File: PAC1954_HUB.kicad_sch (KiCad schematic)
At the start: 11 parts, among them U25 PAC1954T-E_4MX

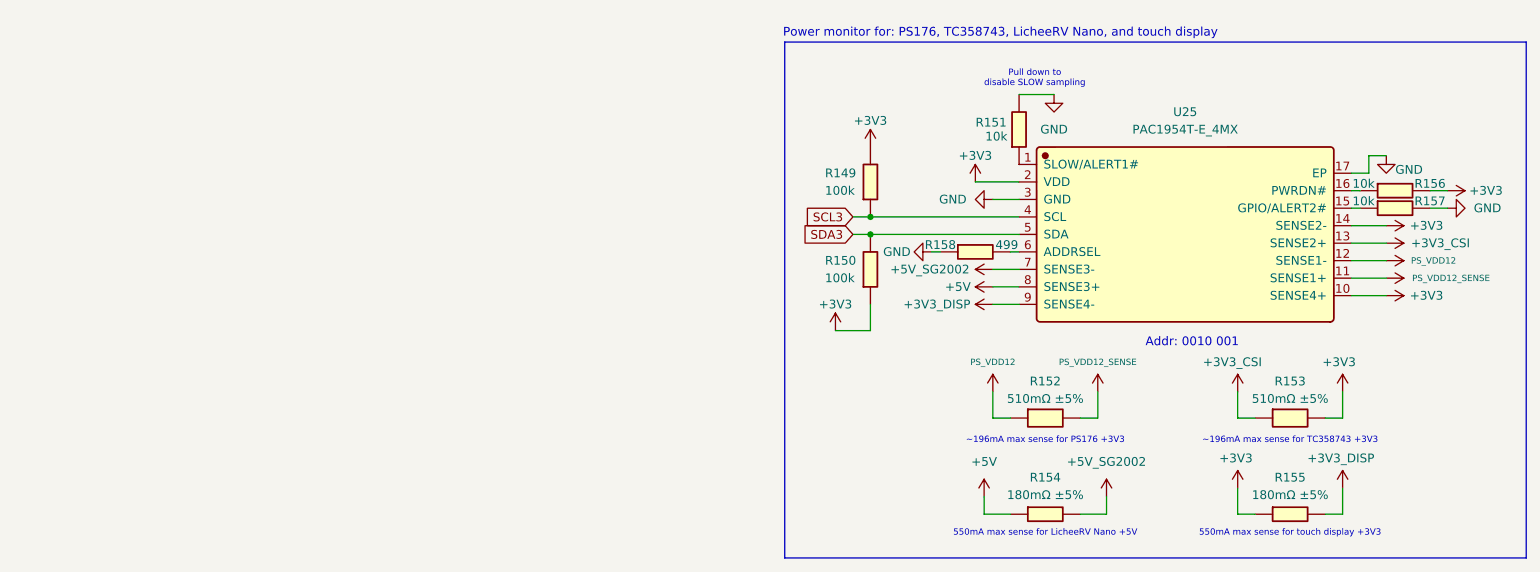
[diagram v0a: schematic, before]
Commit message: Mostly complete initial transfer to hierarchical schematic
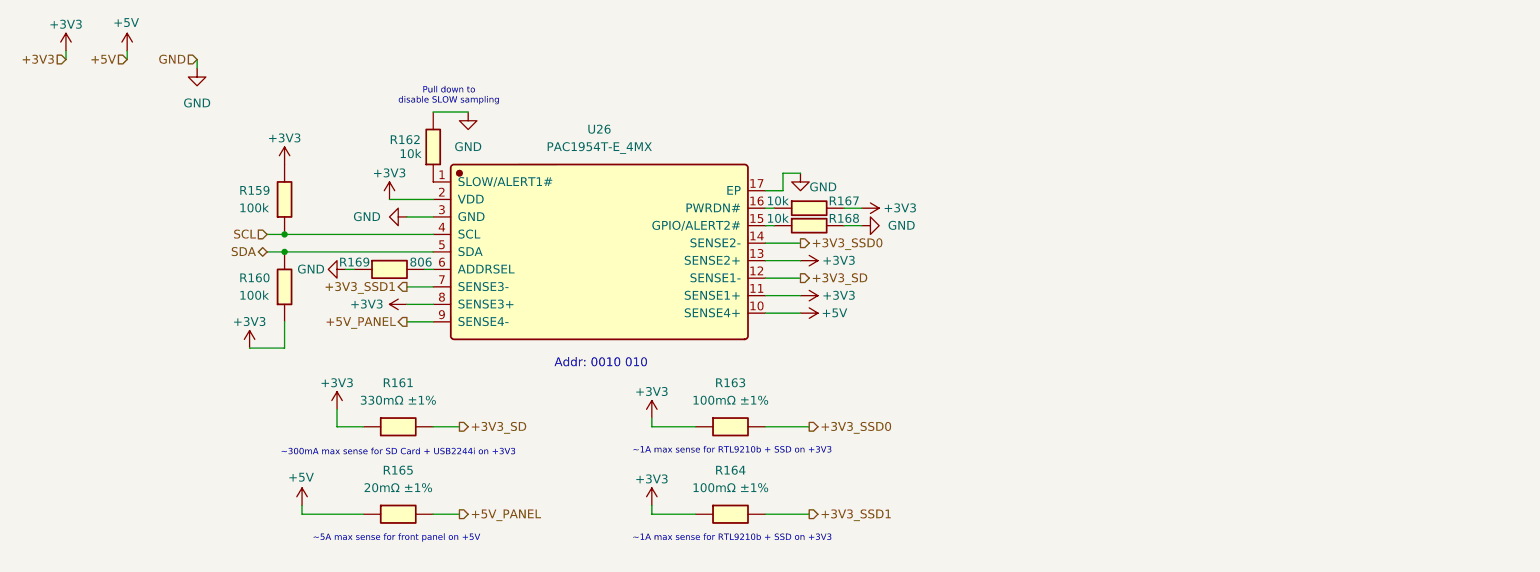
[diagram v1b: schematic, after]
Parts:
- removed R149, R150: 100k, Resistor_SMD:R_0402_1005Metric, symbol JLCImport:0402WGF1003TCE
- removed R151, R156, R157: 10k, Resistor_SMD:R_0402_1005Metric, symbol JLCImport:0402WGF1002TCE
- removed R152, R153: 510mΩ ±5%, Resistor_SMD:R_1210_3225Metric, symbol JLCImport:YHR1206SE1WR003F5
- removed R154, R155: 180mΩ ±5%, Resistor_SMD:R_0508_1220Metric, symbol JLCImport:LTR10EVHJLR18
- removed R158: 499, Resistor_SMD:R_0402_1005Metric, symbol JLCImport:WR04W1R00FTL
- removed U25: PAC1954T-E_4MX, JLCImport:PAC1954T-E_4MX, symbol JLCImport:PAC1954T-E_4MX
- added R159, R160: 100k, Resistor_SMD:R_0402_1005Metric, symbol JLCImport:0402WGF1003TCE
- added R161: 330mΩ ±1%, Resistor_SMD:R_2512_6332Metric, symbol JLCImport:RBJ-12MR330FT
- added R162, R167, R168: 10k, Resistor_SMD:R_0402_1005Metric, symbol JLCImport:0402WGF1002TCE
- added R163, R164: 100mΩ ±1%, Resistor_SMD:R_2512_6332Metric, symbol JLCImport:JER2512F2R100
- added R165: 20mΩ ±1%, Resistor_SMD:R_0603_1608Metric, symbol JLCImport:RBL06FTR020
- added R169: 806, Resistor_SMD:R_0402_1005Metric, symbol JLCImport:CR0402FF8060G
- added U26: PAC1954T-E_4MX, JLCImport:PAC1954T-E_4MX, symbol JLCImport:PAC1954T-E_4MX
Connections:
- net +3V3: now also R159.2, R160.1, R161.1, R163.1, R164.1, R167.2, U26.11 (SENSE1+), U26.13 (SENSE2+), U26.2 (VDD), U26.8 (SENSE3+)
- net +5V: now also R165.1, U26.10 (SENSE4+)
- net GND: now also R162.2, R168.2, R169.1, U26.17 (EP), U26.3 (GND)
- new net: R167.1, U26.16 (PWRDN#)
- new net: R162.1, U26.1 (SLOW/ALERT1#)
- new net: R168.1, U26.15 (GPIO/ALERT2#)
- new net: R169.2, U26.6 (ADDRSEL)
- new net +3V3_SD: R161.2, U26.12 (SENSE1-)
- new net +3V3_SSD0: R163.2, U26.14 (SENSE2-)
- new net +3V3_SSD1: R164.2, U26.7 (SENSE3-)
- new net +5V_PANEL: R165.2, U26.9 (SENSE4-)
- new net SCL: R159.1, U26.4 (SCL)
- new net SDA: R160.2, U26.5 (SDA)
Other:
- note added: "Addr: 0010 010"
- note added: "~1A max sense for RTL9210b + SSD on +3V3"
- note added: "~300mA max sense for SD Card + USB2244i on +3V3"
- note added: "~5A max sense for front panel on +5V"
- note removed: "550mA max sense for LicheeRV Nano +5V"
- note removed: "550mA max sense for touch display +3V3"
- note removed: "Addr: 0010 001"
- note removed: "Power monitor for: PS176, TC358743, LicheeRV Nano, and touch display"
- note removed: "~196mA max sense for PS176 +3V3"
- note removed: "~196mA max sense for TC358743 +3V3"
- company: Designed by: Matthew Kong -> (none)
- title: Temperature and Power monitor sensors -> (none)
